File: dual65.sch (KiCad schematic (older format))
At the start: 21 parts

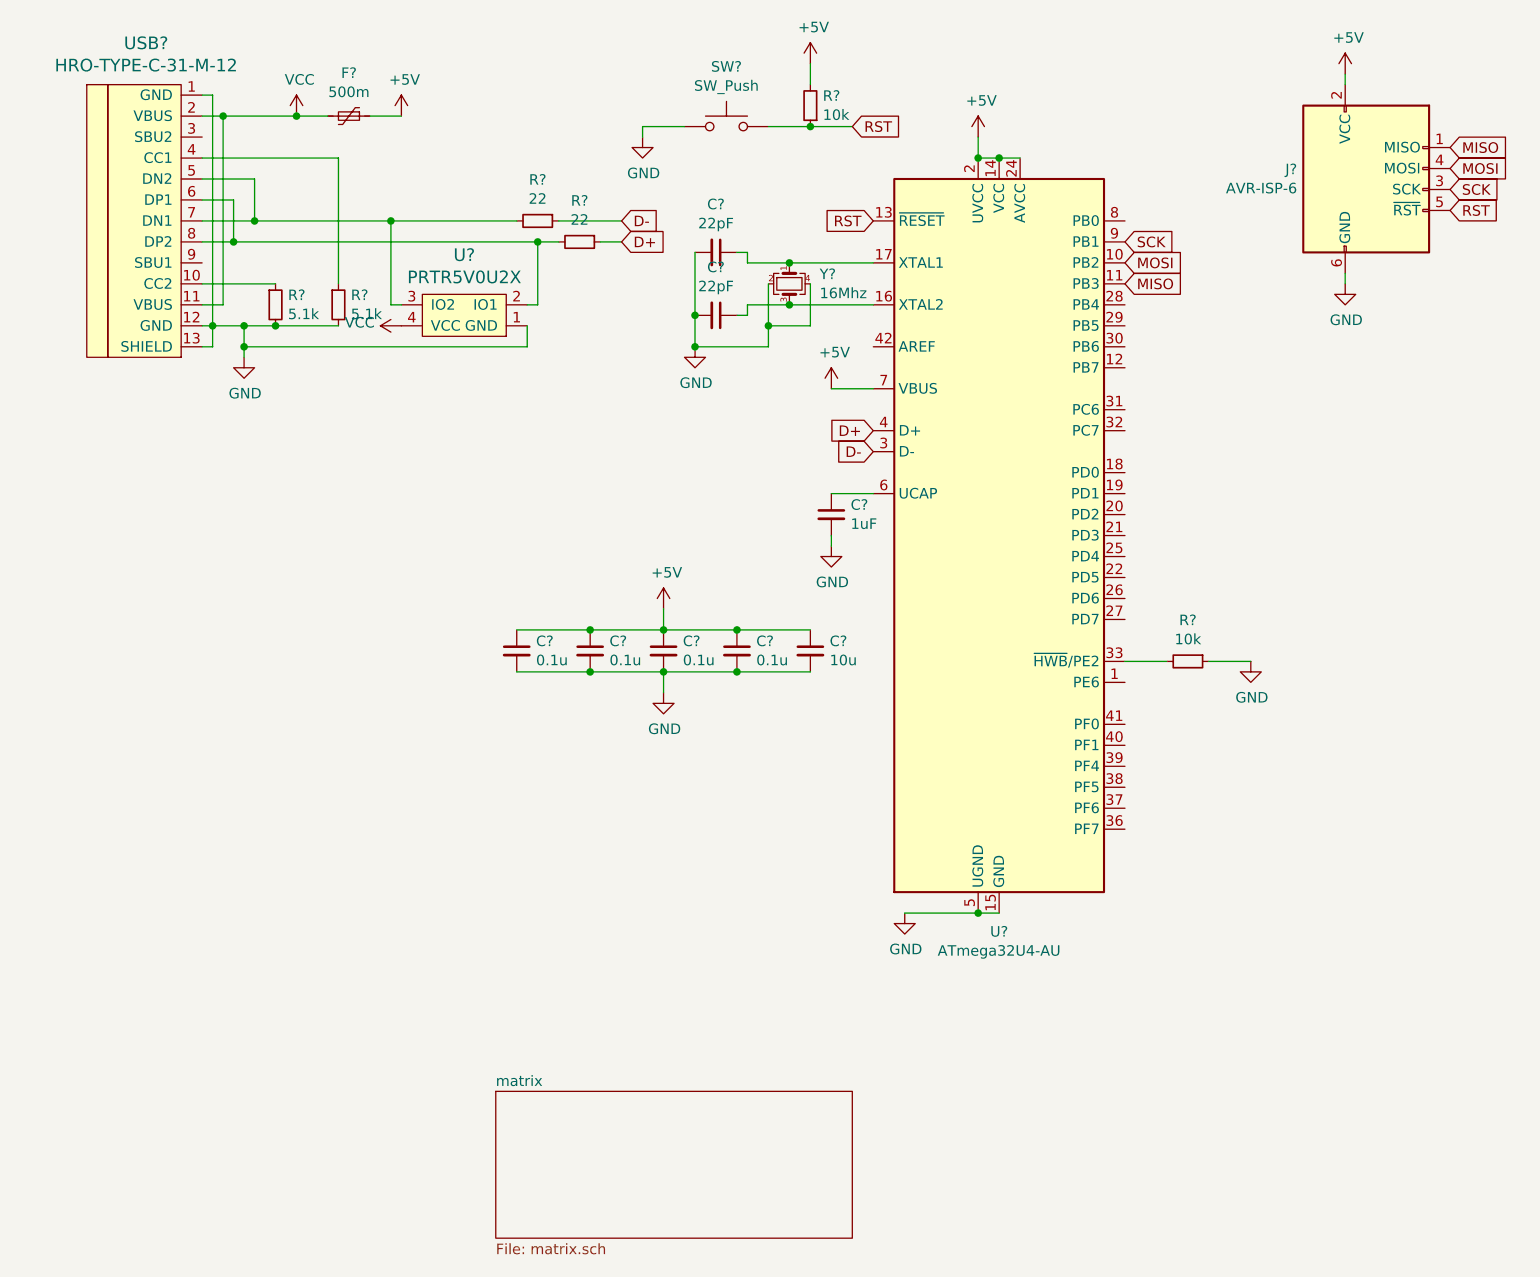
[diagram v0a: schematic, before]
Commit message: finished assign component
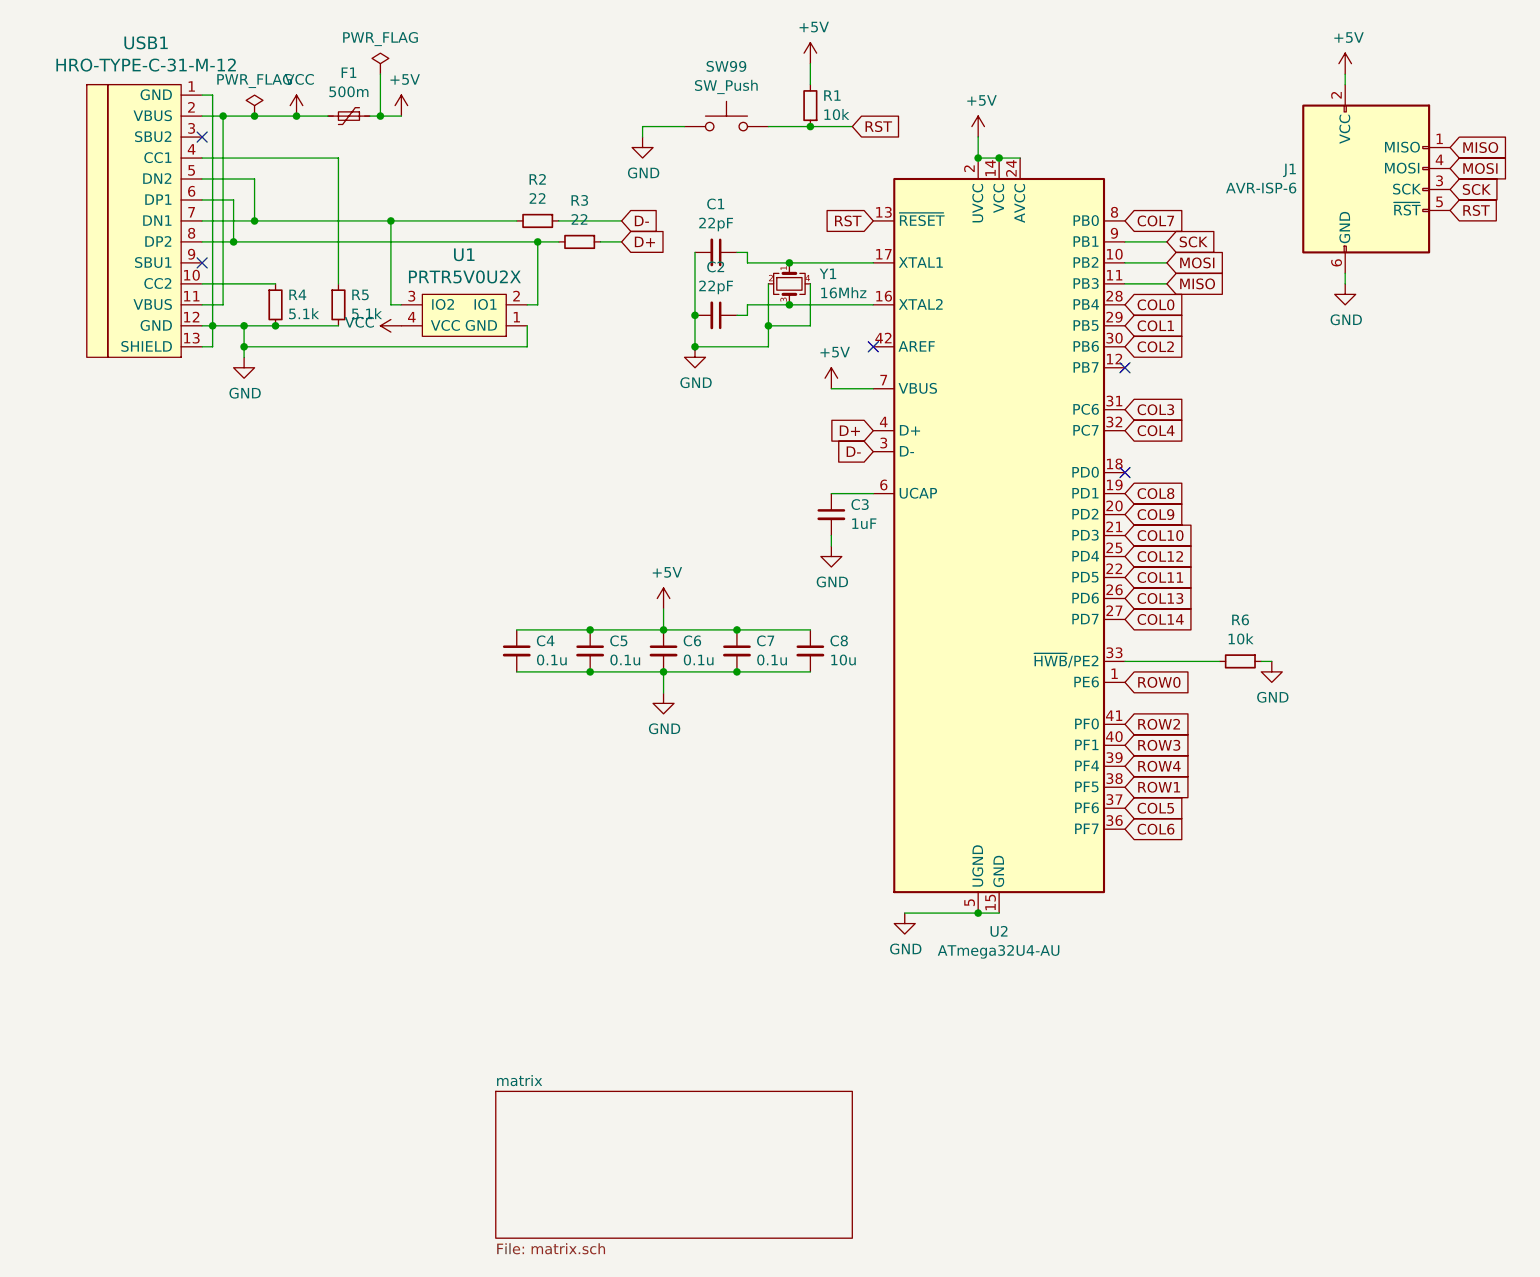
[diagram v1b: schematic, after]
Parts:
- C1, C2, C3, C4, C5, C6, C7: renamed from C?; footprint (none) -> Capacitor_SMD:C_0805_2012Metric_Pad1.18x1.45mm_HandSolder
- C8: renamed from C?; footprint (none) -> Diode_SMD:D_SOD-123
- F1: renamed from F?; footprint (none) -> Fuse:Fuse_1206_3216Metric_Pad1.42x1.75mm_HandSolder
- J1: renamed from J?; footprint (none) -> random-keyboard-parts:Reset_Pretty-Mask
- R1, R2, R3, R4, R5, R6: renamed from R?; footprint (none) -> Resistor_SMD:R_0805_2012Metric_Pad1.20x1.40mm_HandSolder
- SW99: renamed from SW?; footprint (none) -> MX_Only:MXOnly-1U-Hotswap
- U1: renamed from U?; footprint (none) -> random-keyboard-parts:SOT143B
- USB1: renamed from USB?; footprint (none) -> Type-C:HRO-TYPE-C-31-M-12-HandSoldering
- Y1: renamed from Y?; footprint (none) -> Crystal:Crystal_SMD_3225-4Pin_3.2x2.5mm_HandSoldering
- gave numbers to parts that had none: 1
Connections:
- net ROW0: now reaches U2.1 (PE6)
- net COL8: now reaches U2.19 (PD1)
- net COL9: now reaches U2.20 (PD2)
- net COL10: now reaches U2.21 (PD3)
- net COL11: now reaches U2.22 (PD5)
- net COL12: now reaches U2.25 (PD4)
- net COL13: now reaches U2.26 (PD6)
- net COL14: now reaches U2.27 (PD7)
- net COL0: now reaches U2.28 (PB4)
- net COL1: now reaches U2.29 (PB5)
- net COL2: now reaches U2.30 (PB6)
- net COL3: now reaches U2.31 (PC6)
- net COL4: now reaches U2.32 (PC7)
- net COL6: now reaches U2.36 (PF7)
- net COL5: now reaches U2.37 (PF6)
- net ROW1: now reaches U2.38 (PF5)
- net ROW4: now reaches U2.39 (PF4)
- net ROW3: now reaches U2.40 (PF1)
- net ROW2: now reaches U2.41 (PF0)
- net COL7: now reaches U2.8 (PB0)
- no-connect marks 0 -> 5
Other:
- moved on the sheet: R6
